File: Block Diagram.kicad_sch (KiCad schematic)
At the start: 0 parts

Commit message: Update Schematic
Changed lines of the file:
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@@
 		)
 	)
-	(text_box ""
-		(exclude_from_sim no)
-		(at 144.78 358.14 0)
-		(size 70.485 7.62)
-		(margins 1.7144 1.7144 1.7144 1.7144)
-		(stroke
-			(width -0.0001)
-			(type default)
-		)
-		(fill
-			(type color)
-			(color 255 181 181 1)
-		)
-		(effects
-			(font
-				(face "Times New Roman")
-				(size 2.286 2.286)
-				(bold yes)
-				(color 0 0 0 1)
-			)
-		)
-	)
 	(text_box "Temperature & Humidity\n"
 		(exclude_from_sim no)
@@
 		)
 	)
+	(text_box "1x USART Connector"
+		(exclude_from_sim no)
+		(at 187.96 187.96 0)
+		(size 22.86 7.62)
+		(margins 1.7144 1.7144 1.7144 1.7144)
+		(stroke
+			(width -0.0001)
+			(type solid)
+		)
+		(fill
+			(type color)
+			(color 175 92 173 1)
+		)
+		(effects
+			(font
+				(face "Arial")
+				(size 2.286 2.286)
+				(bold yes)
+				(color 255 255 255 1)
+			)
+		)
+	)
 	(text_box "TIM \nCH3,4"
 		(exclude_from_sim no)
@@
 	(text_box ""
 		(exclude_from_sim no)
-		(at 172.72 187.96 0)
-		(size 42.545 7.62)
+		(at 210.82 187.96 0)
+		(size 26.67 7.62)
 		(margins 1.7144 1.7144 1.7144 1.7144)
 		(stroke
@@
 		)
 	)
+	(text_box ""
+		(exclude_from_sim no)
+		(at 166.37 358.14 0)
+		(size 21.59 7.62)
+		(margins 1.7144 1.7144 1.7144 1.7144)
+		(stroke
+			(width -0.0001)
+			(type default)
+		)
+		(fill
+			(type color)
+			(color 255 181 181 1)
+		)
+		(effects
+			(font
+				(face "Times New Roman")
+				(size 2.286 2.286)
+				(bold yes)
+				(color 0 0 0 1)
+			)
+		)
+	)
+	(text_box ""
+		(exclude_from_sim no)
+		(at 152.4 187.96 0)
+		(size 35.56 7.62)
+		(margins 1.7144 1.7144 1.7144 1.7144)
+		(stroke
+			(width -0.0001)
+			(type default)
+		)
+		(fill
+			(type color)
+			(color 255 181 181 1)
+		)
+		(effects
+			(font
+				(face "Times New Roman")
+				(size 2.286 2.286)
+				(bold yes)
+				(color 0 0 0 1)
+			)
+		)
+	)
 	(text_box "DC Gear Motor Connector 2"
 		(exclude_from_sim no)
@@
 		)
 	)
-	(text_box "FDCAN"
+	(text_box "1x USART Connector"
 		(exclude_from_sim no)
-		(at 284.48 172.72 0)
-		(size 12.7 7.62)
+		(at 187.96 358.14 0)
+		(size 22.86 7.62)
 		(margins 1.7144 1.7144 1.7144 1.7144)
 		(stroke
 			(width -0.0001)
-			(type default)
+			(type solid)
 		)
 		(fill
 			(type color)
-			(color 255 170 204 1)
+			(color 175 92 173 1)
 		)
 		(effects
 			(font
-				(face "Times New Roman")
+				(face "Arial")
 				(size 2.286 2.286)
 				(bold yes)
-				(color 0 0 0 1)
+				(color 255 255 255 1)
 			)
 		)
 	)
-	(text_box ""
+	(text_box "FDCAN"
 		(exclude_from_sim no)
-		(at 144.78 195.58 0)
-		(size 27.94 162.56)
+		(at 284.48 172.72 0)
+		(size 12.7 7.62)
 		(margins 1.7144 1.7144 1.7144 1.7144)
 		(stroke
@@
 		(fill
 			(type color)
-			(color 255 181 181 1)
+			(color 255 170 204 1)
 		)
 		(effects
@@
 		)
 	)
-	(text_box "RS-422 Transceiver"
-		(exclude_from_sim no)
-		(at 215.265 187.96 0)
-		(size 22.86 7.62)
-		(margins 1.7144 1.7144 1.7144 1.7144)
-		(stroke
-			(width -0.0001)
-			(type solid)
-		)
-		(fill
-			(type color)
-			(color 175 92 173 1)
-		)
-		(effects
-			(font
-				(face "Arial")
-				(size 2.286 2.286)
-				(bold yes)
-				(color 255 255 255 1)
-			)
-		)
-	)
 	(text_box "GPIO6\n"
 		(exclude_from_sim no)
@@
 		)
 	)
-	(text_box "ADC6"
+	(text_box ""
 		(exclude_from_sim no)
-		(at 312.42 340.36 0)
-		(size 12.7 7.62)
+		(at 152.4 195.58 90)
+		(size 13.97 170.18)
 		(margins 1.7144 1.7144 1.7144 1.7144)
 		(stroke
 			(width -0.0001)
-			(type solid)
+			(type default)
 		)
 		(fill
 			(type color)
-			(color 240 119 110 1)
+			(color 255 181 181 1)
 		)
 		(effects
@@
 		)
 	)
-	(text_box "RS-422 Transceiver"
+	(text_box "ADC6"
 		(exclude_from_sim no)
-		(at 215.265 358.14 0)
-		(size 22.86 7.62)
+		(at 312.42 340.36 0)
+		(size 12.7 7.62)
 		(margins 1.7144 1.7144 1.7144 1.7144)
 		(stroke
@@
 		(fill
 			(type color)
-			(color 175 92 173 1)
+			(color 240 119 110 1)
 		)
 		(effects
 			(font
-				(face "Arial")
+				(face "Times New Roman")
 				(size 2.286 2.286)
 				(bold yes)
-				(color 255 255 255 1)
+				(color 0 0 0 1)
 			)
 		)
@@
 		)
 	)
-	(text_box "1x RS-422 Connector"
-		(exclude_from_sim no)
-		(at 144.78 187.96 0)
-		(size 27.94 7.62)
-		(margins 1.7144 1.7144 1.7144 1.7144)
-		(stroke
-			(width -0.0001)
-			(type default)
-		)
-		(fill
-			(type color)
-			(color 175 92 173 1)
-		)
-		(effects
-			(font
-				(face "Arial")
-				(size 2.286 2.286)
-				(bold yes)
-				(color 255 255 255 1)
-			)
-		)
-	)
 	(text_box "PWM5\n"
 		(exclude_from_sim no)
@@
 	(text_box "USART1"
 		(exclude_from_sim no)
-		(at 238.125 187.96 0)
-		(size 41.275 7.62)
+		(at 237.49 187.96 0)
+		(size 41.91 7.62)
 		(margins 1.7144 1.7144 1.7144 1.7144)
 		(stroke
@@
 				(color 0 0 0 1)
 			)
+		)
+	)
+	(text_box ""
+		(exclude_from_sim no)
+		(at 210.82 358.14 0)
+		(size 27.94 7.62)
+		(margins 1.7144 1.7144 1.7144 1.7144)
+		(stroke
+			(width -0.0001)
+			(type default)
+		)
+		(fill
+			(type color)
+			(color 255 181 181 1)
+		)
+		(effects
+			(font
+				(face "Times New Roman")
+				(size 2.286 2.286)
+				(bold yes)
+				(color 0 0 0 1)
+			)

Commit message: Update Schematic
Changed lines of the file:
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@@
 	(text_box ""
 		(exclude_from_sim no)
-		(at 210.185 172.72 0)
-		(size 5.08 7.62)
+		(at 209.55 172.72 0)
+		(size 29.21 7.62)
 		(margins 1.7144 1.7144 1.7144 1.7144)
 		(stroke
@@
 		(exclude_from_sim no)
 		(at 187.96 187.96 0)
-		(size 22.86 7.62)
+		(size 24.13 7.62)
 		(margins 1.7144 1.7144 1.7144 1.7144)
 		(stroke
@@
 	(text_box ""
 		(exclude_from_sim no)
-		(at 210.82 187.96 0)
-		(size 26.67 7.62)
+		(at 212.09 187.96 0)
+		(size 25.4 7.62)
 		(margins 1.7144 1.7144 1.7144 1.7144)
 		(stroke
@@
 		)
 	)
-	(text_box ""
-		(exclude_from_sim no)
-		(at 210.82 342.9 0)
-		(size 5.08 7.62)
-		(margins 1.7144 1.7144 1.7144 1.7144)
-		(stroke
-			(width -0.0001)
-			(type solid)
-		)
-		(fill
-			(type color)
-			(color 255 170 204 1)
-		)
-		(effects
-			(font
-				(face "Times New Roman")
-				(size 2.286 2.286)
-				(italic yes)
-				(color 0 0 0 1)
-			)
-		)
-	)
 	(text_box "GPIO5\n"
 		(exclude_from_sim no)
@@
 				(bold yes)
 				(color 0 0 0 1)
-			)
-		)
-	)
-	(text_box "Termination Switch"
-		(exclude_from_sim no)
-		(at 187.96 342.9 0)
-		(size 22.86 7.62)
-		(margins 1.7144 1.7144 1.7144 1.7144)
-		(stroke
-			(width -0.0001)
-			(type solid)
-		)
-		(fill
-			(type color)
-			(color 175 92 173 1)
-		)
-		(effects
-			(font
-				(face "Arial")
-				(size 2.286 2.286)
-				(bold yes)
-				(color 255 255 255 1)
 			)
 		)
@@
 		)
 	)
-	(text_box "Termination Switch"
-		(exclude_from_sim no)
-		(at 187.325 172.72 0)
-		(size 22.86 7.62)
-		(margins 1.7144 1.7144 1.7144 1.7144)
-		(stroke
-			(width -0.0001)
-			(type solid)
-		)
-		(fill
-			(type color)
-			(color 175 92 173 1)
-		)
-		(effects
-			(font
-				(face "Arial")
-				(size 2.286 2.286)
-				(bold yes)
-				(color 255 255 255 1)
-			)
-		)
-	)
 	(text_box "Current Sense\n"
 		(exclude_from_sim no)
@@
 	(text_box "FD-CAN Transceiver"
 		(exclude_from_sim no)
-		(at 215.9 342.9 0)
-		(size 22.225 7.62)
+		(at 187.96 342.9 0)
+		(size 22.86 7.62)
 		(margins 1.7144 1.7144 1.7144 1.7144)
 		(stroke
@@
 	(text_box "FDCAN2"
 		(exclude_from_sim no)
-		(at 238.125 342.9 0)
-		(size 41.275 7.62)
+		(at 210.82 342.9 0)
+		(size 68.58 7.62)
 		(margins 1.7144 1.7144 1.7144 1.7144)
 		(stroke
@@
 	(text_box "FD-CAN Transceiver"
 		(exclude_from_sim no)
-		(at 215.265 172.72 0)
+		(at 186.69 172.72 0)
 		(size 22.86 7.62)
 		(margins 1.7144 1.7144 1.7144 1.7144)

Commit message: Update Schematic
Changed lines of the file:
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@@
 		)
 	)
-	(text_box "Page 11"
-		(exclude_from_sim no)
-		(at 350.52 203.2 0)
-		(size 17.78 5.08)
-		(margins 1.7144 1.7144 1.7144 1.7144)
-		(stroke
-			(width -0.0001)
-			(type default)
-		)
-		(fill
-			(type none)
-		)
-		(effects
-			(font
-				(face "Times New Roman")
-				(size 2.286 2.286)
-				(thickness 0.4572)
-				(bold yes)
-				(color 0 0 0 1)
-			)
-			(justify top)
-			(href "#11")
-		)
-	)
 	(text_box "SWD"
 		(exclude_from_sim no)
@@
 		)
 	)
-	(text_box "Page 11"
-		(exclude_from_sim no)
-		(at 350.52 373.38 0)
-		(size 17.78 5.08)
-		(margins 1.7144 1.7144 1.7144 1.7144)
-		(stroke
-			(width -0.0001)
-			(type default)
-		)
-		(fill
-			(type none)
-		)
-		(effects
-			(font
-				(face "Times New Roman")
-				(size 2.286 2.286)
-				(thickness 0.4572)
-				(bold yes)
-				(color 0 0 0 1)
-			)
-			(justify top)
-			(href "#11")
-		)
-	)
 	(text_box "Peak current:"
 		(exclude_from_sim no)
@@
 		)
 	)
-	(text_box "Page #"
-		(exclude_from_sim no)
-		(at 179.07 246.38 0)
-		(size 17.78 5.08)
-		(margins 1.7144 1.7144 1.7144 1.7144)
-		(stroke
-			(width -0.0001)
-			(type default)
-		)
-		(fill
-			(type none)
-		)
-		(effects
-			(font
-				(face "Times New Roman")
-				(size 2.286 2.286)
-				(thickness 0.4572)
-				(bold yes)
-				(color 0 0 0 1)
-			)
-			(justify right top)
-		)
-	)
 	(text_box "4A"
 		(exclude_from_sim no)
@@
 	(text_box "3x MOTOR LEDs"
 		(exclude_from_sim no)
-		(at 342.265 208.28 0)
+		(at 342.9 208.28 0)
 		(size 38.735 7.62)
 		(margins 2.2859 2.2859 2.2859 2.2859)

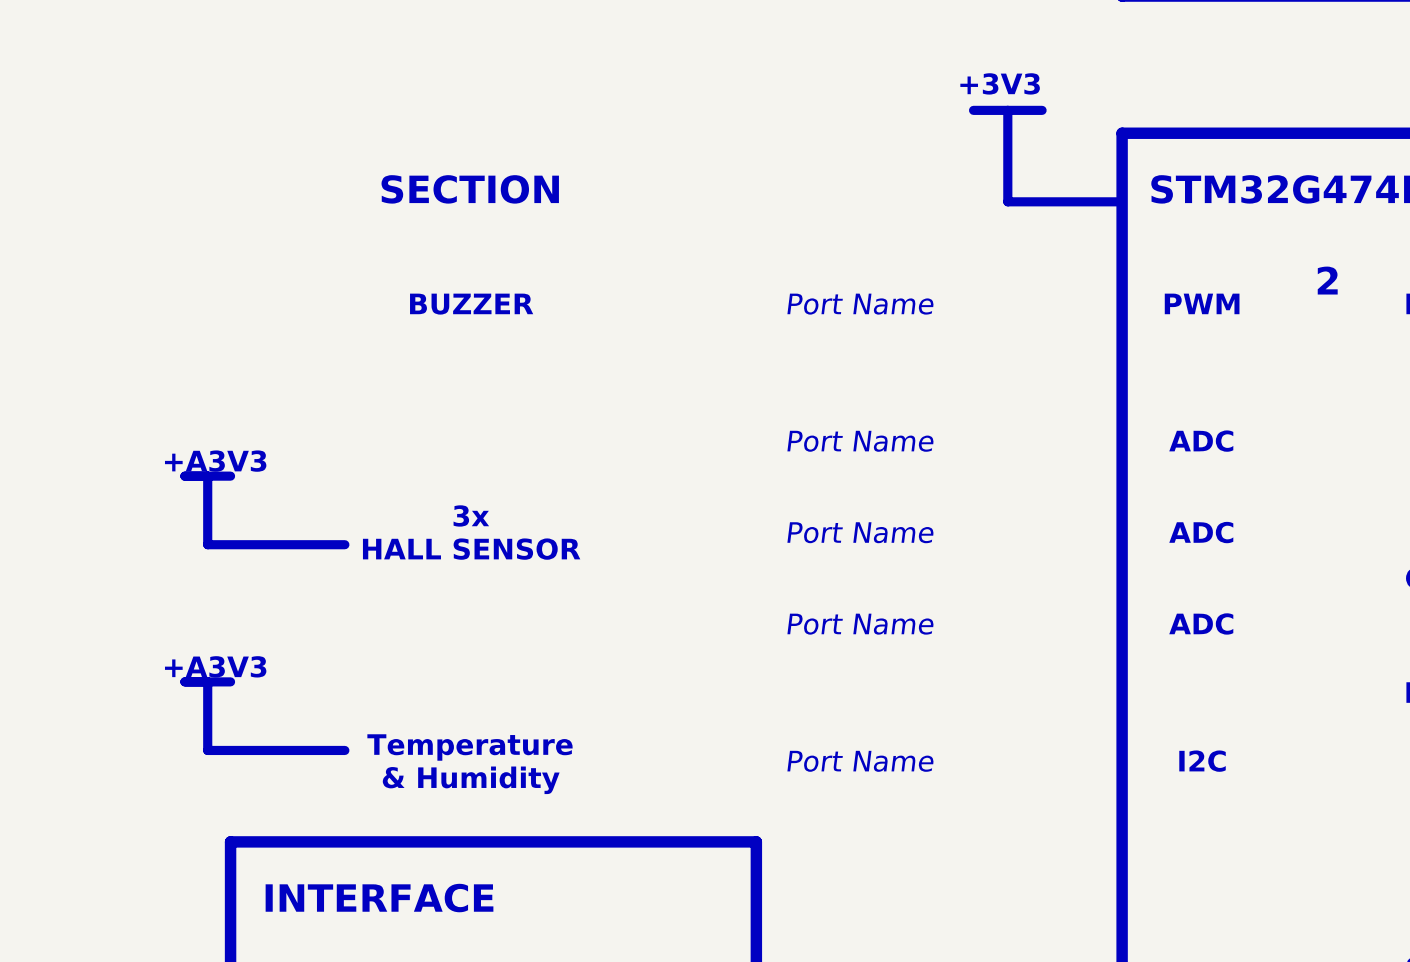
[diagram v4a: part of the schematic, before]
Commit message: Update PCB - Schem - IOC
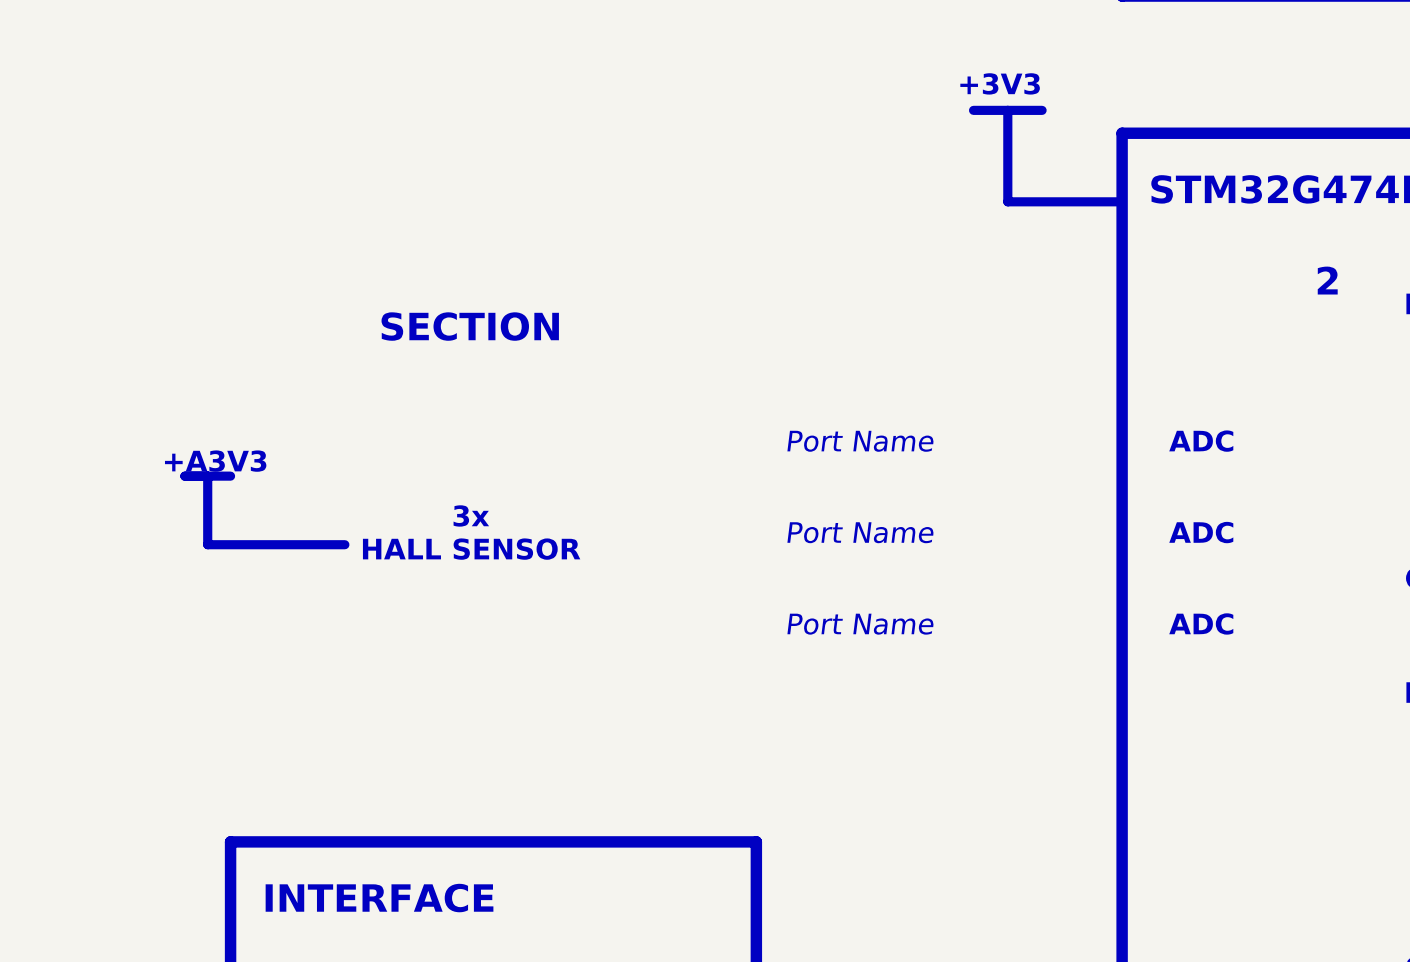
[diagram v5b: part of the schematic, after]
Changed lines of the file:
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@@
 		)
 	)
-	(text "+A3V3"
-		(exclude_from_sim no)
-		(at 175.26 279.4 0)
-		(effects
-			(font
-				(face "Times New Roman")
-				(size 2.286 2.286)
-				(thickness 0.4572)
-				(bold yes)
-				(color 0 0 0 1)
-			)
-			(justify left bottom)
-		)
-	)
 	(text "+5V"
 		(exclude_from_sim no)
@@
 		)
 	)
-	(text_box "BUZZER\n"
-		(exclude_from_sim no)
-		(at 195.58 231.14 0)
-		(size 27.94 12.7)
-		(margins 1.7144 1.7144 1.7144 1.7144)
-		(stroke
-			(width -0.0001)
-			(type solid)
-		)
-		(fill
-			(type color)
-			(color 74 155 203 1)
-		)
-		(effects
-			(font
-				(face "Arial")
-				(size 2.286 2.286)
-				(bold yes)
-				(color 255 255 255 1)
-			)
-		)
-	)
 	(text_box "SWDIO, SWCLK, NRST"
 		(exclude_from_sim no)
@@
 		)
 	)
-	(text_box "Temperature & Humidity\n"
-		(exclude_from_sim no)
-		(at 195.58 281.94 0)
-		(size 27.94 12.7)
-		(margins 1.7144 1.7144 1.7144 1.7144)
-		(stroke
-			(width -0.0001)
-			(type solid)
-		)
-		(fill
-			(type color)
-			(color 74 155 203 1)
-		)
-		(effects
-			(font
-				(face "Arial")
-				(size 2.286 2.286)
-				(bold yes)
-				(color 255 255 255 1)
-			)
-		)
-	)
 	(text_box "M1, M2, C1, C2, VCC, GND"
 		(exclude_from_sim no)
@@
 		)
 	)
-	(text_box "I2C\n"
-		(exclude_from_sim no)
-		(at 284.48 284.48 0)
-		(size 12.7 7.62)
-		(margins 1.7144 1.7144 1.7144 1.7144)
-		(stroke
-			(width -0.0001)
-			(type solid)
-		)
-		(fill
-			(type color)
-			(color 228 41 243 1)
-		)
-		(effects
-			(font
-				(face "Times New Roman")
-				(size 2.286 2.286)
-				(bold yes)
-				(color 0 0 0 1)
-			)
-		)
-	)
 	(text_box "STM32G474RET6\n"
 		(exclude_from_sim no)
@@
 	(text_box "Port Name"
 		(exclude_from_sim no)
-		(at 226.06 284.48 0)
-		(size 53.34 7.62)
-		(margins 1.7144 1.7144 1.7144 1.7144)
-		(stroke
-			(width -0.0001)
-			(type default)
-		)
-		(fill
-			(type color)
-			(color 243 240 160 1)
-		)
-		(effects
-			(font
-				(face "Times New Roman")
-				(size 2.286 2.286)
-				(italic yes)
-				(color 0 0 0 1)
-			)
-		)
-	)
-	(text_box "Port Name"
-		(exclude_from_sim no)
 		(at 330.2 297.18 0)
 		(size 48.26 7.62)
@@
 		)
 	)
-	(text_box "PWM"
-		(exclude_from_sim no)
-		(at 284.48 233.68 0)
-		(size 12.7 7.62)
-		(margins 1.7144 1.7144 1.7144 1.7144)
-		(stroke
-			(width -0.0001)
-			(type solid)
-		)
-		(fill
-			(type color)
-			(color 228 41 243 1)
-		)
-		(effects
-			(font
-				(face "Times New Roman")
-				(size 2.286 2.286)
-				(bold yes)
-				(color 0 0 0 1)
-			)
-		)
-	)
 	(text_box "~200 uF Bulk Capacitance"
 		(exclude_from_sim no)
@@
 		)
 	)
-	(text_box "Port Name"
-		(exclude_from_sim no)
-		(at 226.06 233.68 0)
-		(size 53.34 7.62)
-		(margins 1.7144 1.7144 1.7144 1.7144)
-		(stroke
-			(width -0.0001)
-			(type default)
-		)
-		(fill
-			(type color)
-			(color 243 240 160 1)
-		)
-		(effects
-			(font
-				(face "Times New Roman")
-				(size 2.286 2.286)
-				(italic yes)
-				(color 0 0 0 1)
-			)
-		)
-	)
 	(text_box "MODE, DIAG, OCC, EN"
 		(exclude_from_sim no)
@@
 	(text_box "SECTION"
 		(exclude_from_sim no)
-		(at 195.58 220.98 0)
+		(at 195.58 236.22 0)
 		(size 27.94 7.62)
 		(margins 2.2859 2.2859 2.2859 2.2859)
@@
 	(polyline
 		(pts
-			(xy 180.34 279.4) (xy 180.34 287.02)
-		)
-		(stroke
-			(width 1.016)
-			(type default)
-			(color 162 155 0 1)
-		)
-	)
-	(polyline
-		(pts
 			(xy 83.82 139.7) (xy 98.552 139.7)
 		)
@@
 	(polyline
 		(pts
-			(xy 177.8 279.4) (xy 182.88 279.4)
-		)
-		(stroke
-			(width 1.016)
-			(type default)
-			(color 162 155 0 1)
-		)
-	)
-	(polyline
-		(pts
 			(xy 472.44 114.3) (xy 477.52 114.3)
 		)
@@
 	(polyline
 		(pts
-			(xy 180.34 279.4) (xy 177.8 279.4)
-		)
-		(stroke
-			(width 1.016)
-			(type default)
-			(color 162 155 0 1)
-		)
-	)
-	(polyline
-		(pts
 			(xy 472.44 71.12) (xy 477.52 71.12)
 		)
@@
 		)
 	)
-	(polyline
-		(pts
-			(xy 195.58 287.02) (xy 180.34 287.02)
-		)
-		(stroke
-			(width 1.016)
-			(type default)
-			(color 162 155 0 1)
-		)
-	)
